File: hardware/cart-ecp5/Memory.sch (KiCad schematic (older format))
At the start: 1 part, among them U2 S27KS0641

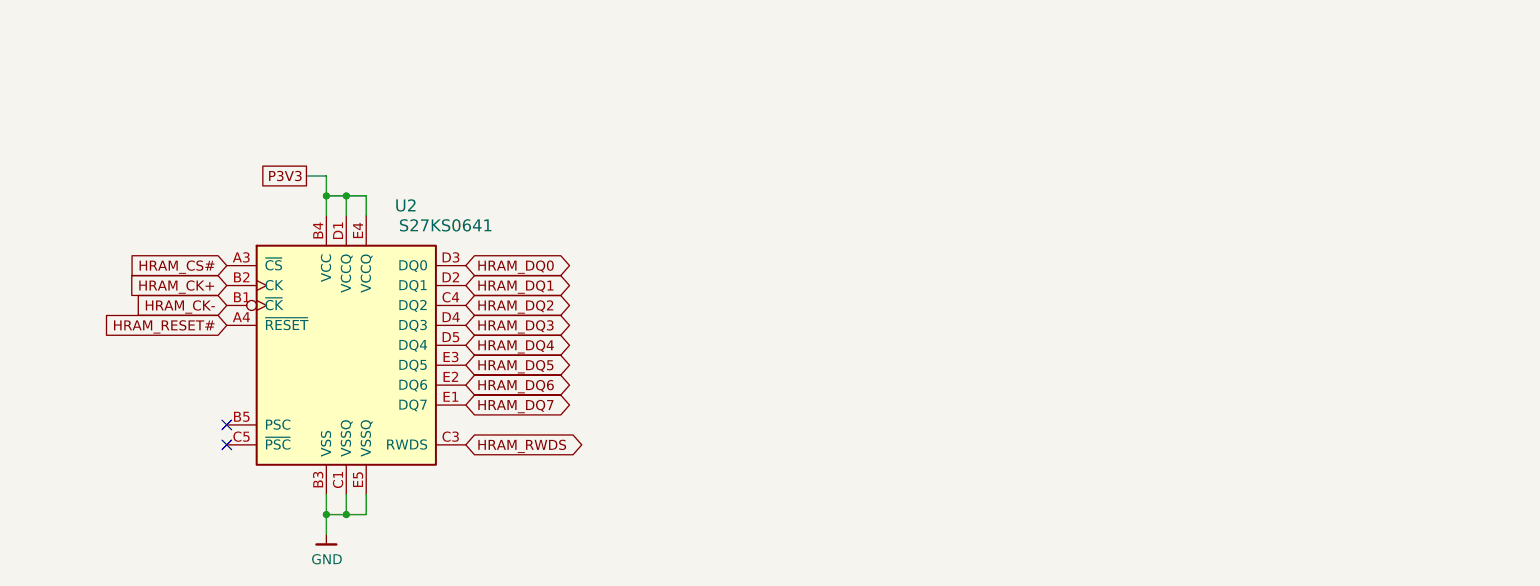
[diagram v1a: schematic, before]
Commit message: Add MicroSD memory to schematic
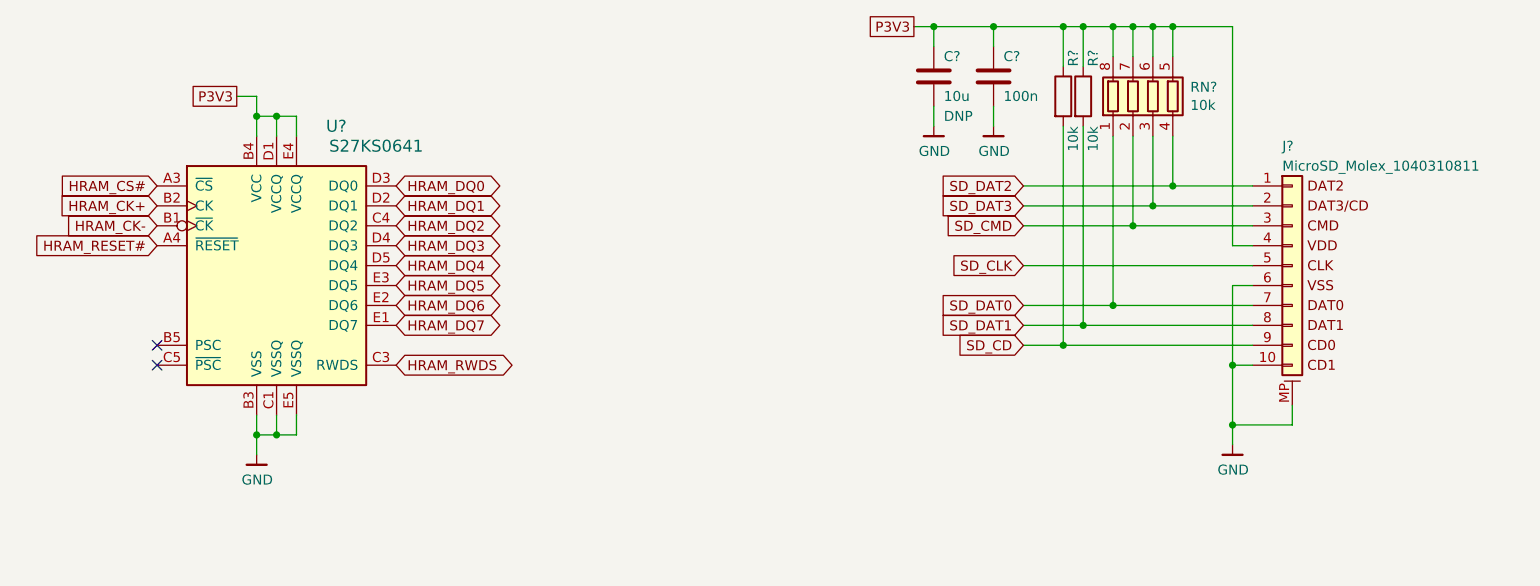
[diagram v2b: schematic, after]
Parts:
- added C16: 10u, Capacitor_SMD:C_0805_2012Metric, symbol Device:C
- added C17: 100n, Capacitor_SMD:C_0603_1608Metric, symbol Device:C
- added J2: MicroSD_Molex_1040310811, ng_conn:MicroSD_Molex_1040310811, symbol ng_conn:MicroSD_Molex_1040310811
- added R1, R8: 10k, Resistor_SMD:R_0603_1608Metric, symbol Device:R
- added RN3: 10k, Resistor_SMD:R_Array_Convex_4x0603, symbol Device:R_Pack04
- renumbered U2 to U?
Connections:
- net GND: now also C16.2, C17.2, J2.10 (DET), J2.6 (Pin_6), J2.MP (MountPin)
- net P3V3: now also C16.1, C17.1, J2.4 (Pin_4), R1.1, R8.1, RN3.5 (R4.2), RN3.6 (R3.2), RN3.7 (R2.2), RN3.8 (R1.2)
- new net SD_CD: J2.9 (Pin_9), R8.2
- new net SD_CLK: J2.5 (Pin_5)
- new net SD_CMD: J2.3 (Pin_3), RN3.2 (R2.1)
- new net SD_DAT0: J2.7 (Pin_7), RN3.1 (R1.1)
- new net SD_DAT1: J2.8 (Pin_8), R1.2
- new net SD_DAT2: J2.1 (Pin_1), RN3.4 (R4.1)
- new net SD_DAT3: J2.2 (Pin_2), RN3.3 (R3.1)
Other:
- moved on the sheet: U?
